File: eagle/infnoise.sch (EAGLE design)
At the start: 25 parts, among them SW1 MC74VHC1G66DFT1G, SW2 MC74VHC1G66DFT1G, X1 USBSMT-MALE

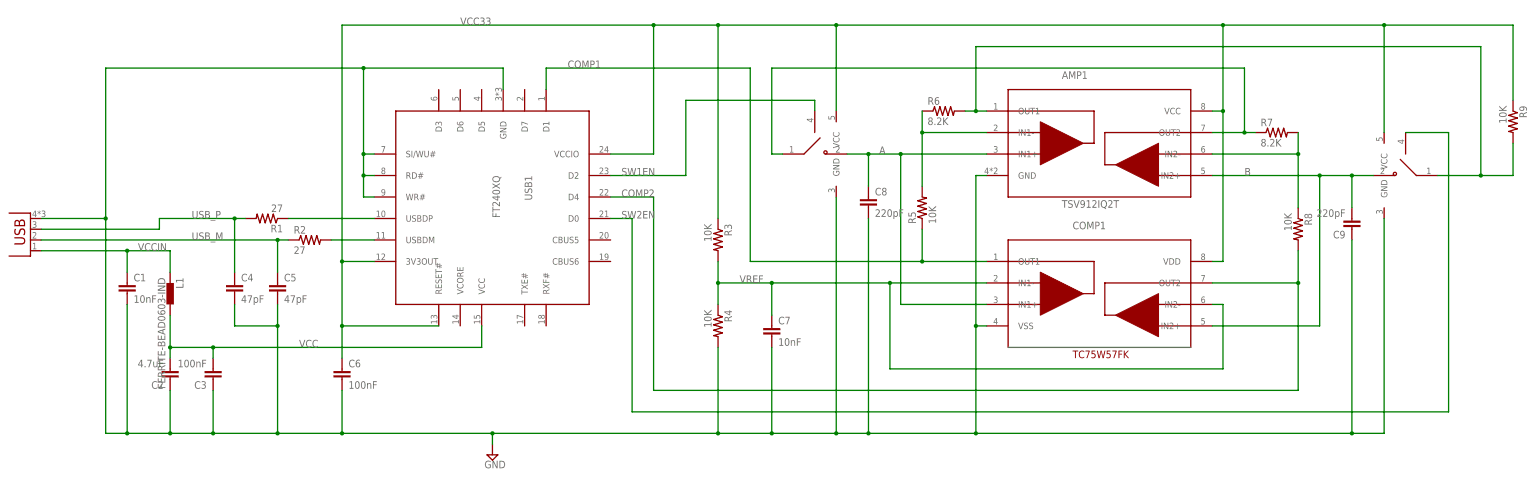
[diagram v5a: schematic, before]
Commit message: Board layout changed
I moved the components on the board around to give a better visual
representation of the components of the infnoise; USB protection,
filter, divider network, and then where the actual magic happens.  Vias
galore, but ERC and DRC satisfied.
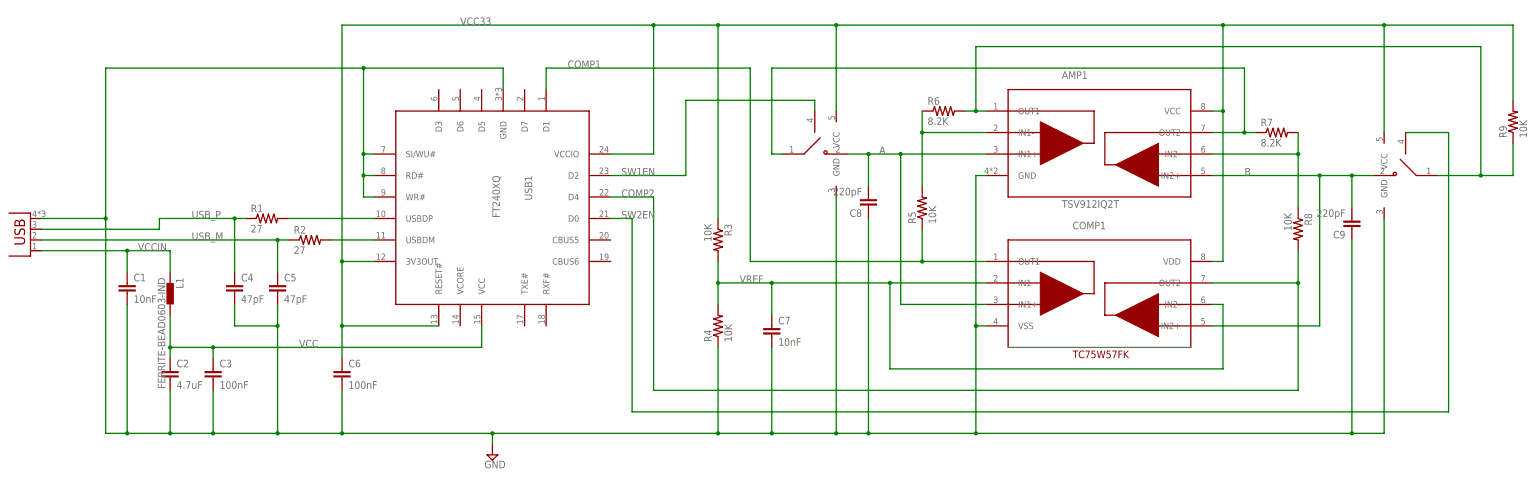
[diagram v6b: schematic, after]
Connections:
- net A: now also C8.2; no longer C8.1
- net AMP1OUT: now also R9.1; no longer R9.2
- net GND: now also C2.2, C3.2, C8.1, R4.1; no longer C2.1, C3.1, C8.2, R4.2
- net N$2: now also R1.2; no longer R1.1
- net USB_P: now also R1.1; no longer R1.2
- net VCC: now also C2.1, C3.1; no longer C2.2, C3.2
- net VCC33: now also R9.2; no longer R9.1
- net VREF: now also R4.2; no longer R4.1
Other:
- moved on the sheet: C2, C3, C8, R1, R4, R9
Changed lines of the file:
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@@
 <instance part="C5" gate="G$1" x="15.24" y="17.78"/>
 <instance part="C6" gate="G$1" x="30.48" y="-2.54"/>
-<instance part="C2" gate="G$1" x="-10.16" y="0" rot="R180"/>
-<instance part="C3" gate="G$1" x="0" y="0" rot="R180"/>
-<instance part="C8" gate="G$1" x="154.94" y="38.1"/>
+<instance part="C2" gate="G$1" x="-10.16" y="-2.54"/>
+<instance part="C3" gate="G$1" x="0" y="-2.54"/>
+<instance part="C8" gate="G$1" x="154.94" y="40.64" rot="R180"/>
 <instance part="C9" gate="G$1" x="269.24" y="35.56" rot="R180"/>
 <instance part="C1" gate="G$1" x="-20.32" y="17.78"/>
 <instance part="L1" gate="G$1" x="-10.16" y="17.78" rot="R270"/>
-<instance part="R1" gate="G$1" x="12.7" y="35.56" rot="R180"/>
+<instance part="R1" gate="G$1" x="12.7" y="35.56"/>
 <instance part="R2" gate="G$1" x="22.86" y="30.48"/>
 <instance part="R6" gate="G$1" x="172.72" y="60.96"/>
@@
 <instance part="R8" gate="G$1" x="256.54" y="33.02" rot="R270"/>
 <instance part="R3" gate="G$1" x="119.38" y="30.48" rot="R270"/>
-<instance part="R4" gate="G$1" x="119.38" y="10.16" rot="R270"/>
+<instance part="R4" gate="G$1" x="119.38" y="10.16" rot="R90"/>
 <instance part="AMP1" gate="G$1" x="208.28" y="50.8"/>
 <instance part="COMP1" gate="G$1" x="208.28" y="15.24"/>
 <instance part="SUPPLY1" gate="GND" x="66.04" y="-20.32"/>
-<instance part="R9" gate="G$1" x="307.34" y="58.42" rot="R270"/>
+<instance part="R9" gate="G$1" x="307.34" y="58.42" rot="R90"/>
 <instance part="SW1" gate="G$1" x="142.24" y="50.8"/>
 <instance part="SW2" gate="G$1" x="281.94" y="45.72" rot="MR0"/>
@@
 <wire x1="5.08" y1="22.86" x2="5.08" y2="35.56" width="0.1524" layer="91"/>
 <label x="-5.08" y="35.56" size="1.778" layer="95"/>
-<pinref part="R1" gate="G$1" pin="2"/>
+<pinref part="R1" gate="G$1" pin="1"/>
 <wire x1="5.08" y1="35.56" x2="7.62" y2="35.56" width="0.1524" layer="91"/>
 <junction x="5.08" y="35.56"/>
@@
 <wire x1="63.5" y1="5.08" x2="0" y2="5.08" width="0.1524" layer="91"/>
 <label x="20.32" y="5.08" size="1.778" layer="95"/>
-<pinref part="C3" gate="G$1" pin="2"/>
+<pinref part="C3" gate="G$1" pin="1"/>
 <wire x1="0" y1="5.08" x2="-10.16" y2="5.08" width="0.1524" layer="91"/>
 <wire x1="0" y1="2.54" x2="0" y2="5.08" width="0.1524" layer="91"/>
-<pinref part="C2" gate="G$1" pin="2"/>
+<pinref part="C2" gate="G$1" pin="1"/>
 <wire x1="-10.16" y1="2.54" x2="-10.16" y2="5.08" width="0.1524" layer="91"/>
 <pinref part="L1" gate="G$1" pin="2"/>
@@
 <wire x1="154.94" y1="-15.24" x2="180.34" y2="-15.24" width="0.1524" layer="91"/>
 <wire x1="180.34" y1="-15.24" x2="269.24" y2="-15.24" width="0.1524" layer="91"/>
-<pinref part="C8" gate="G$1" pin="2"/>
+<pinref part="C8" gate="G$1" pin="1"/>
 <wire x1="269.24" y1="-15.24" x2="276.86" y2="-15.24" width="0.1524" layer="91"/>
 <wire x1="154.94" y1="35.56" x2="154.94" y2="-15.24" width="0.1524" layer="91"/>
@@
 <junction x="35.56" y="50.8"/>
 <junction x="35.56" y="45.72"/>
-<pinref part="C2" gate="G$1" pin="1"/>
+<pinref part="C2" gate="G$1" pin="2"/>
 <wire x1="-10.16" y1="-5.08" x2="-10.16" y2="-15.24" width="0.1524" layer="91"/>
-<pinref part="C3" gate="G$1" pin="1"/>
+<pinref part="C3" gate="G$1" pin="2"/>
 <wire x1="0" y1="-5.08" x2="0" y2="-15.24" width="0.1524" layer="91"/>
 <junction x="-10.16" y="-15.24"/>
@@
 <wire x1="269.24" y1="30.48" x2="269.24" y2="-15.24" width="0.1524" layer="91"/>
 <junction x="269.24" y="-15.24"/>
-<pinref part="R4" gate="G$1" pin="2"/>
+<pinref part="R4" gate="G$1" pin="1"/>
 <wire x1="119.38" y1="5.08" x2="119.38" y2="-15.24" width="0.1524" layer="91"/>
 <junction x="119.38" y="-15.24"/>
@@
 <wire x1="119.38" y1="35.56" x2="119.38" y2="81.28" width="0.1524" layer="91"/>
 <junction x="119.38" y="81.28"/>
-<pinref part="R9" gate="G$1" pin="1"/>
+<pinref part="R9" gate="G$1" pin="2"/>
 <wire x1="307.34" y1="81.28" x2="307.34" y2="63.5" width="0.1524" layer="91"/>
 <label x="58.42" y="81.28" size="1.778" layer="95"/>
@@
 <pinref part="AMP1" gate="G$1" pin="IN1+"/>
 <wire x1="182.88" y1="50.8" x2="162.56" y2="50.8" width="0.1524" layer="91"/>
-<pinref part="C8" gate="G$1" pin="1"/>
+<pinref part="C8" gate="G$1" pin="2"/>
 <wire x1="162.56" y1="50.8" x2="154.94" y2="50.8" width="0.1524" layer="91"/>
 <wire x1="154.94" y1="50.8" x2="149.86" y2="50.8" width="0.1524" layer="91"/>
@@
 <wire x1="299.72" y1="76.2" x2="299.72" y2="45.72" width="0.1524" layer="91"/>
 <junction x="299.72" y="45.72"/>
-<pinref part="R9" gate="G$1" pin="2"/>
+<pinref part="R9" gate="G$1" pin="1"/>
 <wire x1="307.34" y1="53.34" x2="307.34" y2="45.72" width="0.1524" layer="91"/>
 <pinref part="R6" gate="G$1" pin="2"/>
@@
 <junction x="160.02" y="20.32"/>
 <label x="124.46" y="20.32" size="1.778" layer="95"/>
-<pinref part="R4" gate="G$1" pin="1"/>
+<pinref part="R4" gate="G$1" pin="2"/>
 <wire x1="132.08" y1="20.32" x2="119.38" y2="20.32" width="0.1524" layer="91"/>
 <wire x1="119.38" y1="15.24" x2="119.38" y2="20.32" width="0.1524" layer="91"/>
@@
 <net name="N$2" class="0">
 <segment>
-<pinref part="R1" gate="G$1" pin="1"/>
+<pinref part="R1" gate="G$1" pin="2"/>
 <pinref part="USB1" gate="G$1" pin="USBDP"/>
 <wire x1="17.78" y1="35.56" x2="38.1" y2="35.56" width="0.1524" layer="91"/>

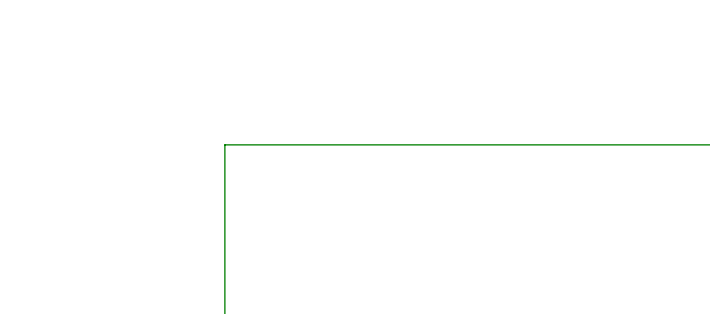
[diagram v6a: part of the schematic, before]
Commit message: Added 3 fiducial marks on the board
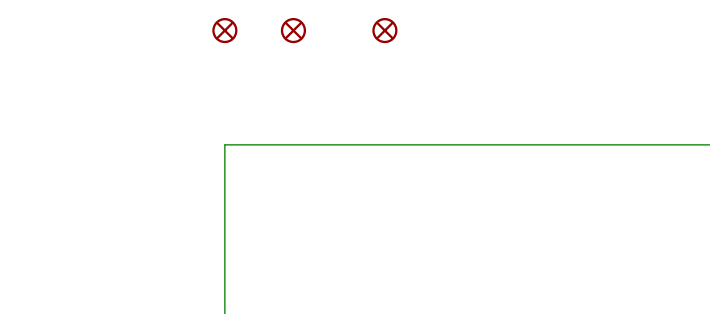
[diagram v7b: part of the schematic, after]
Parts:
- added FID1, FID2, FID3: FIDUCIALUFIDUCIAL, SparkFun-Aesthetics:FIDUCIALUFIDUCIAL
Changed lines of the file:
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@@
 <?xml version="1.0" encoding="utf-8"?>
 <!DOCTYPE eagle SYSTEM "eagle.dtd">
-<eagle version="6.5.0">
+<eagle version="7.1.0">
 <drawing>
 <settings>
@@
 <layer number="48" name="Document" color="7" fill="1" visible="no" active="no"/>
 <layer number="49" name="Reference" color="7" fill="1" visible="no" active="no"/>
+<layer number="50" name="dxf" color="7" fill="1" visible="no" active="no"/>
 <layer number="51" name="tDocu" color="7" fill="1" visible="no" active="no"/>
 <layer number="52" name="bDocu" color="7" fill="1" visible="no" active="no"/>
+<layer number="53" name="tGND_GNDA" color="7" fill="9" visible="no" active="no"/>
+<layer number="54" name="bGND_GNDA" color="1" fill="9" visible="no" active="no"/>
+<layer number="56" name="wert" color="7" fill="1" visible="no" active="no"/>
 <layer number="90" name="Modules" color="5" fill="1" visible="yes" active="yes"/>
 <layer number="91" name="Nets" color="2" fill="1" visible="yes" active="yes"/>
@@
 <layer number="97" name="Info" color="7" fill="1" visible="yes" active="yes"/>
 <layer number="98" name="Guide" color="6" fill="1" visible="yes" active="yes"/>
+<layer number="100" name="Muster" color="7" fill="1" visible="no" active="no"/>
+<layer number="101" name="Patch_Top" color="12" fill="4" visible="yes" active="yes"/>
+<layer number="102" name="Vscore" color="7" fill="1" visible="yes" active="yes"/>
+<layer number="103" name="tMap" color="7" fill="1" visible="yes" active="yes"/>
+<layer number="104" name="Name" color="16" fill="1" visible="yes" active="yes"/>
+<layer number="105" name="tPlate" color="7" fill="1" visible="yes" active="yes"/>
+<layer number="106" name="bPlate" color="7" fill="1" visible="yes" active="yes"/>
+<layer number="107" name="Crop" color="7" fill="1" visible="yes" active="yes"/>
+<layer number="108" name="tplace-old" color="10" fill="1" visible="no" active="yes"/>
+<layer number="109" name="ref-old" color="11" fill="1" visible="no" active="yes"/>
+<layer number="116" name="Patch_BOT" color="9" fill="4" visible="yes" active="yes"/>
+<layer number="121" name="_tsilk" color="7" fill="1" visible="yes" active="yes"/>
+<layer number="122" name="_bsilk" color="7" fill="1" visible="yes" active="yes"/>
+<layer number="125" name="_tNames" color="7" fill="1" visible="yes" active="yes"/>
+<layer number="144" name="Drill_legend" color="7" fill="1" visible="yes" active="yes"/>
+<layer number="151" name="HeatSink" color="7" fill="1" visible="yes" active="yes"/>
+<layer number="199" name="Contour" color="7" fill="1" visible="yes" active="yes"/>
+<layer number="200" name="200bmp" color="1" fill="10" visible="yes" active="yes"/>
+<layer number="201" name="201bmp" color="2" fill="10" visible="yes" active="yes"/>
+<layer number="202" name="202bmp" color="3" fill="10" visible="yes" active="yes"/>
+<layer number="203" name="203bmp" color="4" fill="10" visible="yes" active="yes"/>
+<layer number="204" name="204bmp" color="5" fill="10" visible="yes" active="yes"/>
+<layer number="205" name="205bmp" color="6" fill="10" visible="yes" active="yes"/>
+<layer number="206" name="206bmp" color="7" fill="10" visible="yes" active="yes"/>
+<layer number="207" name="207bmp" color="8" fill="10" visible="yes" active="yes"/>
+<layer number="208" name="208bmp" color="9" fill="10" visible="yes" active="yes"/>
+<layer number="209" name="209bmp" color="7" fill="1" visible="yes" active="yes"/>
+<layer number="210" name="210bmp" color="7" fill="1" visible="yes" active="yes"/>
+<layer number="211" name="211bmp" color="7" fill="1" visible="yes" active="yes"/>
+<layer number="212" name="212bmp" color="7" fill="1" visible="yes" active="yes"/>
+<layer number="213" name="213bmp" color="7" fill="1" visible="yes" active="yes"/>
+<layer number="214" name="214bmp" color="7" fill="1" visible="yes" active="yes"/>
+<layer number="215" name="215bmp" color="7" fill="1" visible="yes" active="yes"/>
+<layer number="216" name="216bmp" color="7" fill="1" visible="yes" active="yes"/>
+<layer number="217" name="217bmp" color="18" fill="1" visible="no" active="no"/>
+<layer number="218" name="218bmp" color="19" fill="1" visible="no" active="no"/>
+<layer number="219" name="219bmp" color="20" fill="1" visible="no" active="no"/>
+<layer number="220" name="220bmp" color="21" fill="1" visible="no" active="no"/>
+<layer number="221" name="221bmp" color="22" fill="1" visible="no" active="no"/>
+<layer number="222" name="222bmp" color="23" fill="1" visible="no" active="no"/>
+<layer number="223" name="223bmp" color="24" fill="1" visible="no" active="no"/>
+<layer number="224" name="224bmp" color="25" fill="1" visible="no" active="no"/>
+<layer number="250" name="Descript" color="3" fill="1" visible="no" active="no"/>
+<layer number="251" name="SMDround" color="12" fill="11" visible="no" active="no"/>
+<layer number="254" name="cooling" color="7" fill="1" visible="yes" active="yes"/>
 </layers>
 <schematic xreflabel="%F%N/%S.%C%R" xrefpart="/%S.%C%R">
@@
 <part name="X1" library="infnoise" deviceset="USB" device="SMT-MALE"/>
 <part name="C7" library="infnoise" deviceset="CAP" device="0603-CAP" value="10nF"/>
+<part name="FID1" library="SparkFun-Aesthetics" deviceset="FIDUCIAL" device="UFIDUCIAL"/>
+<part name="FID2" library="SparkFun-Aesthetics" deviceset="FIDUCIAL" device="UFIDUCIAL"/>
+<part name="FID3" library="SparkFun-Aesthetics" deviceset="FIDUCIAL" device="UFIDUCIAL"/>
 </parts>
 <sheets>
@@
 <instance part="X1" gate="G$1" x="-43.18" y="35.56" rot="R180"/>
 <instance part="C7" gate="G$1" x="132.08" y="7.62"/>
+<instance part="FID1" gate="G$1" x="-25.4" y="83.82"/>
+<instance part="FID2" gate="G$1" x="-17.78" y="83.82"/>
+<instance part="FID3" gate="G$1" x="-7.62" y="83.82"/>
 </instances>
 <busses>
